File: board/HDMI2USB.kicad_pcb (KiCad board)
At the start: 10 copper layers, 337 parts, among them J1 USB_MICRO_B, P3 CONN_7X2, SW1 SW_PUSH, U1 MT41J128M16, U10 XC6SLX150T, U16 ΜA78L00, U17 FXO-HC536R, U18 FXO-HC536R, U19 FXO-HC536R, U20 KSZ9031RNX, U3 W25Q128FVEIG

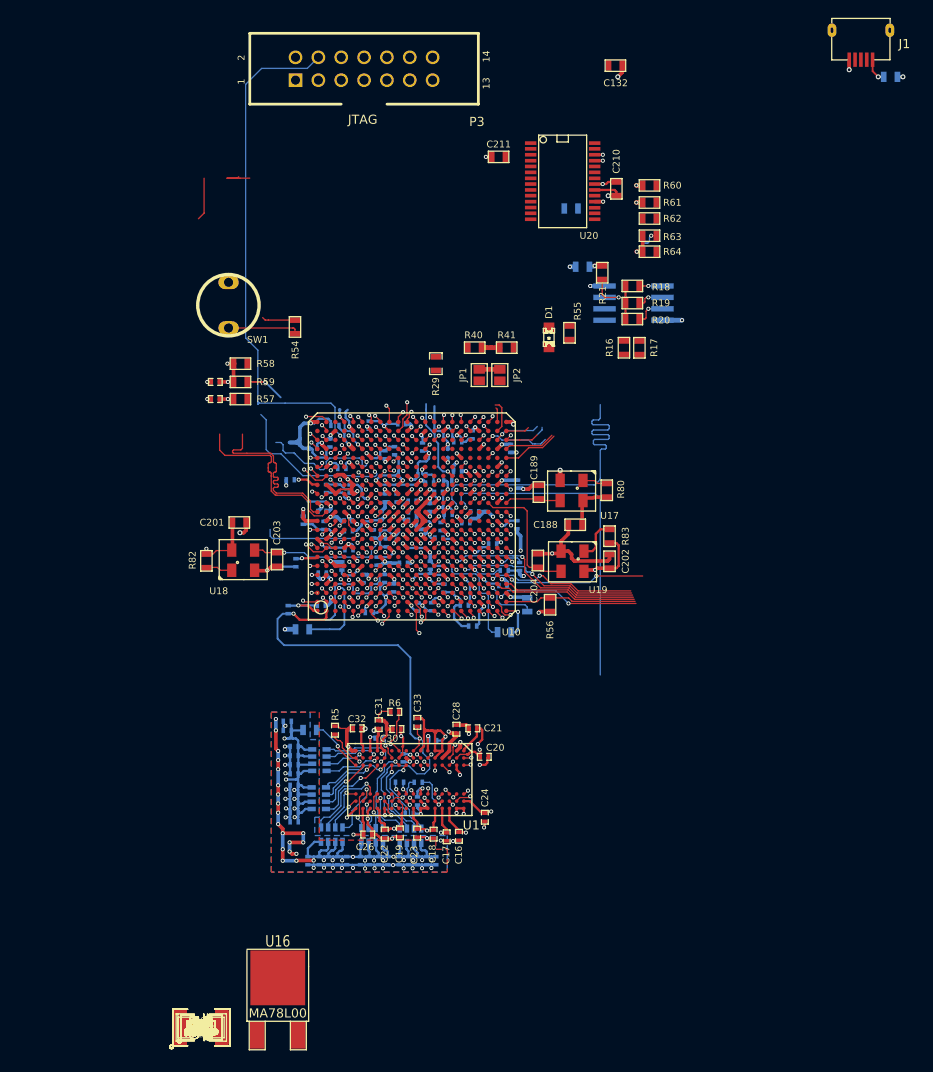
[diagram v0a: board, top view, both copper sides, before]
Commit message: Issue #1458 - HDMI RX TX pins added, Cypress added, DDR added
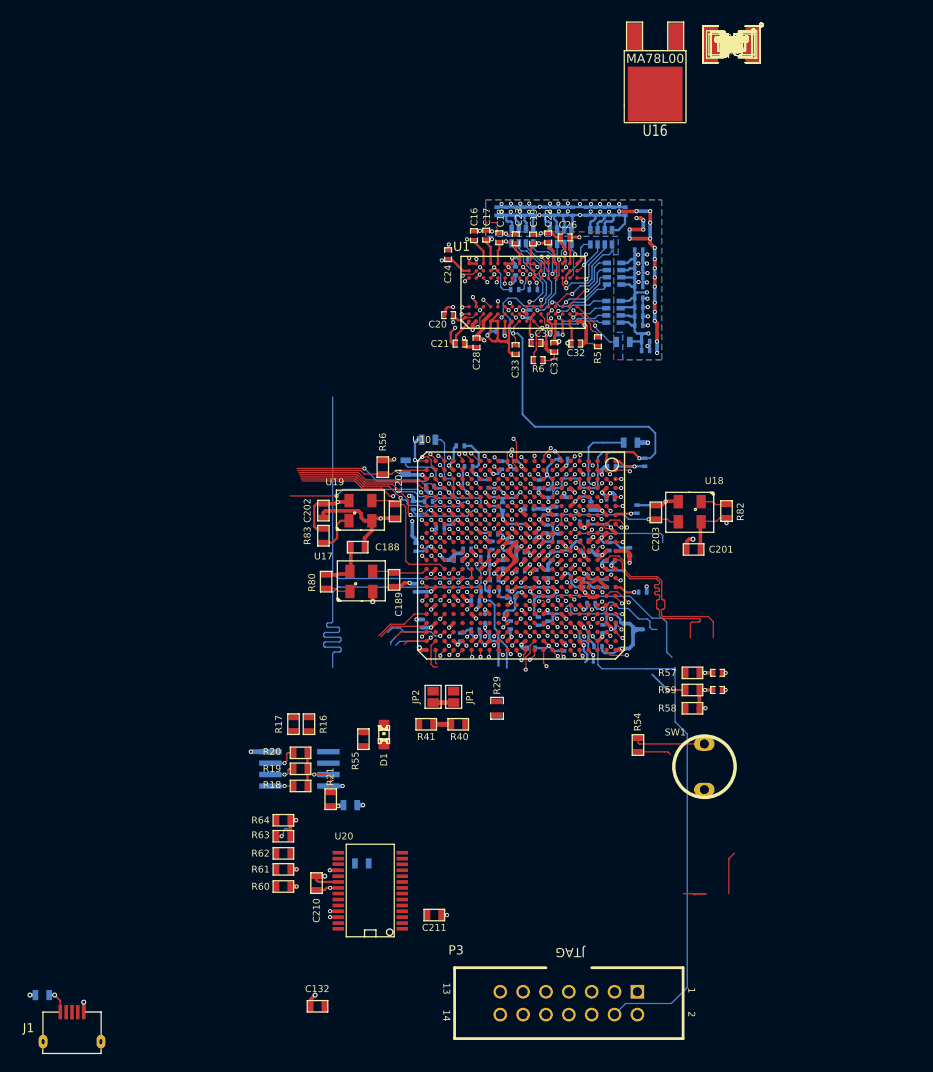
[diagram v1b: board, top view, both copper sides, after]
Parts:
- moved J1 142.6 mm to (162.8, 226.1), turned to 0 degrees
- moved R22 138.9 mm to (159.5, 220.9), turned to 0 degrees
- moved C133 124.2 mm to (236.1, 115.3), turned to 180 degrees
- moved C134 124.2 mm to (236.1, 115.3), turned to 180 degrees
- moved C135 124.2 mm to (236.1, 115.3), turned to 180 degrees
- moved C136 124.2 mm to (236.1, 115.3), turned to 180 degrees
- moved C137 124.2 mm to (236.1, 115.3), turned to 180 degrees
- moved C138 124.2 mm to (236.1, 115.3), turned to 180 degrees
- moved C139 124.2 mm to (236.1, 115.3), turned to 180 degrees
- moved C140 124.2 mm to (236.1, 115.3), turned to 180 degrees
- moved C141 124.2 mm to (236.1, 115.3), turned to 180 degrees
- moved C142 124.2 mm to (236.1, 115.3), turned to 180 degrees
- moved C143 124.2 mm to (236.1, 115.3), turned to 180 degrees
- moved C144 124.2 mm to (236.1, 115.3), turned to 180 degrees
- moved C145 124.2 mm to (236.1, 115.3), turned to 180 degrees
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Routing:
- net (no net): track 2011.9 -> 2009.5 mm

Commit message: Issue #1481 - DOC
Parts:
- removed R68: 100R, SM0402
- added D2: LED, DO214, F.Cu at (48.5, -14.2)
- added J2: HDMI, HDMI_TH, F.Cu at (195.6, 232.4)
- added J3: HDMI, HDMI_TH, F.Cu at (222.0, 232.4)
- added J4: HDMI, HDMI_TH, F.Cu at (139.4, 232.2)
- added J5: HDMI, HDMI_TH, F.Cu at (167.1, 232.4)
- added J6: RJ45(HFJ11-1GO1ERL), RJ45_10P-10C, F.Cu at (243.1, 82.3)
- added L1: INDUCTOR, SM0805, F.Cu at (212.1, 89.7)
- added L2: 7.2uH, IND202, F.Cu at (125.2, -24.1)
- added L4: 1.5UH, IND202, F.Cu at (60.2, -47.8)
- added L5: 1.5UH, IND202, F.Cu at (44.7, -26.2)
- added L6: INDUCTOR, SM0805, F.Cu at (212.1, 79.2)
- added L7: INDUCTOR, SM0805, F.Cu at (212.1, 84.3)
- added P1: CONN_2, pin_array_6x2_SMD, F.Cu at (40.8, -39.1)
- added P4: CONN_1, FX18_120, F.Cu at (37.7, -75.3)
- added P5: CONN_1, FX18_120, F.Cu at (37.2, -89.0)
- added P6: CONN_1, DIP-SMD_2X2, F.Cu at (108.0, -13.7)
- added R116: 10K, SM0603, F.Cu at (-24.9, 69.6)
- added R124: 50R, SM0603, F.Cu at (219.2, 205.2)
- added R125: 50R, SM0603, F.Cu at (217.2, 205.2)
- added R126: 100K, SM0603, F.Cu at (161.8, 208.8)
- added R127: 100K, SM0603, F.Cu at (191.8, 209.0)
- added R128: 50R, SM0603, F.Cu at (-4.83, 58.4)
- added R129: 47K, SM0603, F.Cu at (161.8, 206.5)
- added R130: 47K, SM0603, F.Cu at (189.7, 209.0)
- added R131: 50R, SM0603, F.Cu at (215.1, 205.2)
- added R132: 100K, SM0603, F.Cu at (213.4, 210.1)
- added R133: 47K, SM0603, F.Cu at (161.8, 204.5)
- added R134: 47K, SM0603, F.Cu at (187.7, 209.0)
- added R135: 47K, SM0603, F.Cu at (215.4, 210.1)
- added R136: 47K, SM0603, F.Cu at (217.4, 210.1)
- added R137: 1.5K, SM0603, F.Cu at (187.7, 205.2)
- added R138: 1.5K, SM0603, F.Cu at (158.5, 209.0)
- added R139: 1.5K, SM0603, F.Cu at (189.7, 205.2)
- added R140: 1.5K, SM0603, F.Cu at (158.5, 207.0)
- added R141: 1.5K, SM0603, F.Cu at (229.1, 208.5)
- added R142: 1.5K, SM0603, F.Cu at (227.1, 208.5)
- added R143: 27K, SM0603, F.Cu at (192.0, 205.2)
- added R144: 27K, SM0603, F.Cu at (158.5, 205.0)
- added R145: 50R, SM0603, F.Cu at (226.8, 205.2)
- added R146: 27K, SM0603, F.Cu at (231.1, 208.5)
- added R147: 50R, SM0603, F.Cu at (228.9, 205.2)
- added R148: 15K, SM0603, F.Cu at (194.1, 205.2)
- added R149: 15K, SM0603, F.Cu at (158.5, 202.9)
- added R150: 50R, SM0603, F.Cu at (230.9, 205.2)
- added R151: 15K, SM0603, F.Cu at (233.2, 208.5)
- added R152: 50R, SM0603, F.Cu at (232.9, 205.2)
- added R153: 1K, SM0603, F.Cu at (232.9, 229.9)
- added R188: 50R, SM0603, F.Cu at (129.8, 211.8)
- added R189: 50R, SM0603, F.Cu at (129.8, 209.8)
- added R190: 50R, SM0603, F.Cu at (129.8, 207.8)
- added R191: 50R, SM0603, F.Cu at (129.8, 205.7)
- added R192: 100K, SM0603, F.Cu at (125.2, 215.4)
- added R193: 47K, SM0603, F.Cu at (125.2, 217.4)
- added R194: 47K, SM0603, F.Cu at (125.2, 219.7)
- added R196: 1.5K, SM0603, F.Cu at (119.9, 223.5)
- added R197: 1.5K, SM0603, F.Cu at (119.6, 225.8)
- added R198: 50R, SM0603, F.Cu at (124.7, 223.8)
- added R199: 27K, SM0603, F.Cu at (119.6, 227.8)
- added R200: 50R, SM0603, F.Cu at (124.7, 225.8)
- added R201: 50R, SM0603, F.Cu at (124.7, 227.8)
- added R203: 50R, SM0603, F.Cu at (124.7, 230.1)
- added R204: 15K, SM0603, F.Cu at (119.6, 230.1)
- added R205: 1K, SM0603, F.Cu at (143.5, 225.8)
- added R66: 4.7K, SM0603, F.Cu at (235.7, 105.4)
- added R67: 4.7K, SM0603, F.Cu at (235.7, 109.2)
- added R72: 0R, SM0402, F.Cu at (35.3, -59.7)
- added R73: 390R, SM0603, F.Cu at (252.7, 113.3)
- added R74: 4.7K, SM0603, F.Cu at (252.7, 111.5)
- added R92: 330R, SM0603, F.Cu at (253.5, 78.2)
- added R93: 10K, SM0603, F.Cu at (-24.9, 63.0)
- added U11: MICRO_SD, MicroSD, F.Cu at (349.9, 32.3)
- added U12: TPS51200, BGA96-0.8, F.Cu at (28.0, -23.0)
- added U13: IP4776CZ38, SSOP38_N, F.Cu at (165.9, 217.9)
- added U14: IP4776CZ38, SSOP38_N, F.Cu at (194.1, 217.4)
- added U15: IP4776CZ38, SSOP38_N, F.Cu at (221.2, 217.7)
- added U2: CY7C68013A_100AC, PCI-EXPRESS, F.Cu at (-2.24, 75.7)
- added U21: IP4776CZ38, SSOP38_N, F.Cu at (138.4, 217.9)
- added U22: ΜA78L00, SSOP28, F.Cu at (-10.2, 46.0)
- added U4: GBU15005-G, PDSO_G14, F.Cu at (108.7, -40.6)
- added U5: 7805, PDSO_G14, F.Cu at (80.8, -43.9)
- added U6: TPS54560, SMAJACKRightAngled, F.Cu at (25.9, -41.7)
- added U7: TPS53319, DQP-22, F.Cu at (59.4, -28.2)
- added U8: TPS54625, PDSO_G14, F.Cu at (76.5, -25.9)
- added U9: TPS54625, SON_10, F.Cu at (59.7, -13.5)
- C201, C202, C53, C58: value 0.1UF -> 0.1MFD
- C203: value 15PF -> 4.7uF; footprint SM0603 -> SM0805
- C204: value 15PF -> 1uF; footprint SM0603 -> SM0805
- C210, C211: value 100nF -> 4.7uF; footprint SM0603 -> SM0805
- C212: value 100nF -> 4.7uF; footprint SM1210 -> SM0805
- C214, C217, C218, C219, C230: footprint SM1210 -> SM0805
- C216: value 100nF -> 27pF; footprint SM1210 -> SM0603
- C220: value 4.7uF -> 100nF; footprint SM1812 -> SM0805
- C222: value 100nF -> 0.1uF; footprint SM1812 -> SM0603
- C223: footprint SM0603 -> SM0805
- C225: value 100nF -> 4.7uF; footprint SM1812 -> SM0805
- C226, C229: footprint SM1210 -> SM0603; moved to B.Cu
- C227: footprint SM1812 -> SM0805
- C231: value 12pF -> 100nF; footprint SM1812 -> SM0805
- C232: value 12pF -> 100nF; footprint SM0805 -> SM0603; moved to B.Cu
- C233, C234: footprint SM0805 -> SM0603; moved to B.Cu
- C235: value 100nF -> 12pF; footprint SM0805 -> SM0603
- C238: value 100nF -> 12pF; footprint SM0402 -> SM0603
- C239: footprint SM0402 -> SM0603
- C39, C40, C41, C42: value 0.1MFD -> 0.1uFD
- C43, C44: value 12pF -> 0.1MFD
- C46, C49, C50: value 10UF -> 47uF
- C47: value 10UF -> 4.7uF
- C52: value 1UF -> 0.1MFD
- C54: value 8.2NF -> 0.1MFD
- C62: value 0.1UF -> 12pF
- C64: value 47UF -> 12pF
- C66: value 47UF -> 0.1MFD
- R13: value 10K -> 8.06K
- R14: value 10K -> 100R
- R15: value 10K -> 330R
- R16, R17: value R -> 50R
- R18, R19, R20, R21: value R -> 10K
- R22: value 4.7K -> 1K; moved to F.Cu
- R23, R24, R26: value 75R -> 100R
- R25: value 75R -> 100K
- R27, R28: value 75R -> 330R
- R30: value 75R -> 20K
- R31: value 75R -> 1.5K
- R32, R35, R36: value 75R -> 10K
- R33, R34: value 75R -> 2.2K
- R37, R49, R51: value 75R -> 4.7K
- R38: value 10K -> 39K
- R39: value 10K -> 27K
- R42, R43: value 1.5K -> 0R
- R44, R45: value 10K -> 0R
- R46: value 2.2K -> 0R
- R47: value 75R -> 0R
- R48: value 75R -> 4.7K; footprint SM0402 -> SM0603
- R50: value 2.2K -> 1.5K
- R65: value 100R -> 4.7K
- R69: value 100R -> 2.49K; footprint SM0402 -> SM0603
- R70: value 330R -> 390R; footprint SM0402 -> SM0603
- R71: value 330R -> 4.7K; footprint SM0402 -> SM0603
- R75: value 10K -> 4.7K; footprint SM0402 -> SM0603
- R76: value 100K -> 100R
- R81: value 21.5K -> 100R
- R82, R83: value 4K7 -> 100R
- R84: value 22.1K -> 100K; moved to B.Cu
- R88: value 0.03E -> 100K; moved to B.Cu
- R89: value 0.03E -> 330R
- U18: value FXO-HC536R -> USB3340
- U19: value FXO-HC536R -> MCP1825; footprint FXO-HC536R -> SOT223-5
- U20: value KSZ9031RNX -> RTL8211E-VB; footprint SSOP28 -> QFN48(RTL8211E)
- moved C40 187.1 mm to (75.2, 19.8)
- moved C42 180.8 mm to (82.5, 19.8)
- moved C41 177.0 mm to (82.5, 27.2)
- moved C44 172.5 mm to (92.5, 19.8)
- moved C63 168.9 mm to (91.9, 27.2)
- moved C37 166.7 mm to (99.8, 19.3)
- moved C65 162.7 mm to (99.8, 26.4)
- moved C38 161.5 mm to (106.4, 19.1)
- moved C179 156.3 mm to (121.7, 221.7)
- moved R88 150.7 mm to (143.5, 234.2)
- moved C76 149.6 mm to (121.9, 18.5)
- moved C185 145.5 mm to (143.5, 227.6)
- moved C133 142.8 mm to (121.4, 30.1)
- moved C134 142.8 mm to (121.4, 30.1)
- moved C135 142.8 mm to (121.4, 30.1)
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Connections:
- net /Cypress/D_N renamed /USB/USB_DM
- net /Cypress/D_P renamed /USB/USB_DP
- net N-00000500 renamed /USB/U1-SCL
- C136 pad 1: DDR1V8 -> VCC1V5
- C138 pad 2: DDR1V8 -> VCC1V5
- C154 pad 1: /Power/VCC3V3_RS+ -> VCC3V3
- C155 pad 2: /Power/DDR1V8_RS+ -> VCC1V5
- C156 pad 2: /Power/DDR0V9_RS+ -> VTTDDR0
- C157 pad 2: /Power/VCC3V3_RS+ -> VCC3V3
- C158 pad 1: /Power/VCC1V2_RS+ -> VCC1V2
- C159 pad 2: /Power/DDR0V9_RS+ -> VTTDDR0
- C160 pad 2: /Power/VCC3V3_RS+ -> VCC3V3
- C161 pad 2: /Power/DDR1V8_RS+ -> VCC1V5
- C162 pad 2: /Power/DDR0V9_RS+ -> VTTDDR0
- C163 pad 2: /Power/VCC3V3_RS+ -> VCC3V3
- C164 pad 2: /Power/VCC1V2_RS+ -> VCC1V2
- C165 pad 2: /Power/DDR1V8_RS+ -> VCC1V5
- C166 pad 2: /Power/DDR0V9_RS+ -> VTTDDR0
- C167 pad 2: /Power/VCC1V2_RS+ -> VCC1V2
- C168 pad 2: /Power/DDR0V9_RS+ -> VTTDDR0
- C189 pad 2: /SPI_Flash/USRCLK -> /FPGA_Bank_1_2/USRCLK
- C201 pad 1: GND -> VCC3V3
- C201 pad 2: VCC3V3 -> GND
- C202 pad 1: GND -> VCC3V3
- C202 pad 2: VCC3V3 -> GND
- C203 pad 1: GND -> /Ethernet/VCC3V3
- C203 pad 2: /SPI_Flash/CLK2 -> GND
- C204 pad 1: GND -> /Ethernet/VCC1V0
- C204 pad 2: /SPI_Flash/CLK1 -> GND
- C210 pad 1: /Ethernet/VCC1V2 -> /Ethernet/VCC3V3
- C211 pad 1: /Ethernet/VCC1V2 -> /Ethernet/VCC3V3
- C212 pad 1: /Ethernet/VCC1V2 -> /Ethernet/VCC1V0
- C214 pad 1: /Ethernet/VCC1V2 -> /Ethernet/ETH_VCC3V3
- C216 pad 1: /Ethernet/AVDDL -> GND
- C216 pad 2: GND -> /Ethernet/ETH_RXCLK
- C217 pad 1: /Ethernet/PLL1V2 -> /Ethernet/VCC3V3
- C218 pad 1: /Ethernet/VCC1V2 -> /Ethernet/VCC3V3
- C219 pad 1: /Ethernet/AVDDL -> /Ethernet/ETH_VCC3V3
- C220 pad 1: /Ethernet/PLL1V2 -> /Ethernet/ETH_VCC3V3
- C222 pad 1: /Ethernet/VCC1V2 -> /Ethernet/ETH_RESET_B
- C223 pad 1: /Ethernet/AVDDL -> /Ethernet/ETH_VCC1V0
- C224 pad 1: /Ethernet/AVDDH -> /Ethernet/AVDD3V3
- C225 pad 1: /Ethernet/DVDDH -> /Ethernet/ETH_VCC3V3
- C226 pad 1: /Ethernet/AVDDH -> /Ethernet/ETH_VCC1V0
- C227 pad 1: /Ethernet/DVDDH -> /Ethernet/AVDD3V3
- C228 pad 1: /Ethernet/AVDDH -> /Ethernet/ETH_VCC3V3
- C229 pad 1: /Ethernet/DVDDH -> /Ethernet/ETH_VCC1V0
- C230 pad 1: /Ethernet/AVDDH -> /Ethernet/AVDD3V3
- C231 pad 1: /Ethernet/XTAL2 -> /Ethernet/ETH_VCC3V3
- C232 pad 1: /Ethernet/XTAL1 -> /Ethernet/ETH_VCC1V0
- C233 pad 1: GND -> /Ethernet/ETH_VCC1V0
- C233 pad 2: N-00000461 -> GND
- C234 pad 1: GND -> /Ethernet/ETH_VCC1V0
- C234 pad 2: N-00000460 -> GND
- C235 pad 1: GND -> /Ethernet/XTAL2_50MHZ
- C235 pad 2: N-00000459 -> GND
- C238 pad 1: GND -> /Ethernet/XTAL1_50MHZ
- C238 pad 2: N-00000458 -> GND
- C239 pad 1: /Ethernet/C_GND -> /Ethernet/VCC3V3
- C34 pad 1: VCC3V3 -> N-00000381
- C35 pad 1: VCC3V3 -> N-00000381
- C37 pad 1: VCC3V3 -> GND
- C37 pad 2: GND -> N-00000375
- C38 pad 1: VCC3V3 -> N-00000364
- C43 pad 1: GND -> VCC3V3
- C43 pad 2: N-00000503 -> GND
- C44 pad 1: N-00000502 -> VCC3V3
- C46 pad 1: VCC12V0 -> GND
- C46 pad 2: GND -> N-00000399
- C47 pad 2: VCC12V0 -> N-00000399
- C49 pad 2: VCC12V0 -> VCC5V0
- C50 pad 1: VCC12V0 -> GND
- C50 pad 2: GND -> VCC5V0
- C52 pad 1: GND -> VCC3V3
- C52 pad 2: N-00000539 -> GND
- C53 pad 1: VCC12V0 -> VCC3V3
- C54 pad 1: GND -> VCC3V3
- C54 pad 2: N-00000531 -> GND
- C58 pad 1: N-00000511 -> VCC3V3
- C58 pad 2: N-00000510 -> GND
- C62 pad 1: N-00000527 -> GND
- C62 pad 2: /Power/VCC5V0_RS+ -> /USB/XTALIN
- C64 pad 1: GND -> /USB/XTALIOUT
- C64 pad 2: /Power/VCC5V0_RS+ -> GND
- C66 pad 1: GND -> VCC3V3
- C66 pad 2: /Power/VCC5V0_RS+ -> GND
- C76 pad 2: DDR1V8 -> VCC1V5
- J1 pad 4: (no net) -> /USB/ID
- P3 pad 10: (no net) -> N-00000159
- P3 pad 4: (no net) -> N-00000152
- P3 pad 6: (no net) -> N-00000155
- P3 pad 8: (no net) -> N-00000157
- R13 pad 1: VCC3V3 -> GND
- R13 pad 2: N-00000492 -> N-00000365
- R14 pad 1: VCC3V3 -> N-00000374
- R14 pad 2: N-00000507 -> /FPGA_Power/TDO_FPGA/TDO-JTAG
- R15 pad 1: VCC3V3 -> N-00000369
- R15 pad 2: N-00000491 -> /FPGA_Power/PROG_B
- R16 pad 2: (no net) -> /FPGA_Bank_1_2/SPI_DO_DIN_MISO1
- R17 pad 2: (no net) -> /FPGA_Bank_1_2/SPI_D1_MISO2
- R18 pad 2: /SPI_Flash/SPI_CS_N -> /FPGA_Bank_1_2/SPI_CS_N
- R21 pad 1: /SPI_Flash/SPI_D2_MISO3 -> /FPGA_Bank_1_2/SPI_D2_MISO3
- R22 pad 1: GND -> N-00000337
- R22 pad 2: N-00000442 -> /Ethernet/VCC3V3
- R23 pad 2: (no net) -> /USB/TDO-USB/TDI-FPGA
- R24 pad 2: (no net) -> /FPGA_Power/TMS
- R25 pad 2: (no net) -> GND
- R26 pad 2: (no net) -> /FPGA_Power/TCK
- R27 pad 2: (no net) -> /FPGA_Power/INIT_B
- R28 pad 2: (no net) -> /FPGA_Power/DONE
- R30 pad 2: (no net) -> N-00000364
- R31 pad 2: (no net) -> N-00000373
- R32 pad 1: N-00000492 -> N-00000362
- R32 pad 2: (no net) -> GND
- R33 pad 1: N-00000491 -> /USB/U1-SDA
- R33 pad 2: (no net) -> VCC3V3
- R34 pad 2: (no net) -> VCC3V3
- R35 pad 1: N-00000498 -> N-00000343
- R35 pad 2: (no net) -> VCC3V3
- R36 pad 1: N-00000499 -> GND
- R36 pad 2: (no net) -> N-00000344
- R37 pad 1: N-00000490 -> N-00000363
- R37 pad 2: (no net) -> GND
- R38 pad 1: GND -> N-00000336
- R38 pad 2: N-00000490 -> /Ethernet/VCC1V0
- R39 pad 2: N-00000501 -> N-00000336
- R42 pad 1: N-00000505 -> /Ethernet/ETH_RXD0
- R42 pad 2: N-00000507 -> N-00000343
- R43 pad 1: N-00000506 -> /Ethernet/ETH_RXD1
- R43 pad 2: N-00000501 -> N-00000329
- R44 pad 1: VCC3V3 -> /Ethernet/ETH_RXD2
- R44 pad 2: /Cypress/U1-SLWR -> N-00000328
- R45 pad 1: VCC3V3 -> /Ethernet/ETH_RXD3
- R45 pad 2: /Cypress/U1-SLRD -> N-00000318
- R46 pad 1: /Cypress/U1-SCL -> /Ethernet/ETH_RXCTL
- R46 pad 2: VCC3V3 -> N-00000311
- R47 pad 1: N-00000480 -> (no net)
- R47 pad 2: (no net) -> N-00000317
- R48 pad 1: N-00000479 -> GND
- R48 pad 2: (no net) -> /Ethernet/ETH_RXCTL
- R49 pad 1: N-00000485 -> /Ethernet/ETH_VCC3V3
- R49 pad 2: (no net) -> /Ethernet/ETH_RXD0
- R50 pad 1: /Cypress/U1-SDA -> /Ethernet/ETH_VCC3V3
- R50 pad 2: VCC3V3 -> /Ethernet/ETH_MDIO
- R51 pad 1: (no net) -> /Ethernet/ETH_RESET_B
- R51 pad 2: N-00000496 -> /Ethernet/VCC3V3
- R52 pad 2: (no net) -> /FPGA_Power/INIT_B
- R56 pad 1: /FPGA_Power/FPGA_PROG_B -> /FPGA_Power/PROG_B
- R60 pad 1: /SPI_Flash/SD_DAT2 -> /FPGA_Bank_1_2/SD_DAT2
- R61 pad 1: /SPI_Flash/SD_DAT3 -> /FPGA_Bank_1_2/SD_DAT3
- R62 pad 1: /SPI_Flash/SD_CMD -> /FPGA_Bank_1_2/SD_CMD
- R63 pad 1: /SPI_Flash/SD_DAT0 -> /FPGA_Bank_1_2/SD_DAT0
- R64 pad 1: /SPI_Flash/SD_DAT1 -> /FPGA_Bank_1_2/SD_DAT1
- R65 pad 1: N-00000477 -> /Ethernet/ETH_VCC3V3
- R65 pad 2: (no net) -> /Ethernet/ETH_RXD1
- R69 pad 1: N-00000471 -> N-00000311
- R69 pad 2: (no net) -> GND
- R70 pad 1: N-00000473 -> N-00000321
- R70 pad 2: (no net) -> /Ethernet/LED0
- R71 pad 1: N-00000469 -> N-00000321
- R71 pad 2: (no net) -> /Ethernet/VCC3V3
- R75 pad 1: VCC12V0 -> N-00000331
- R75 pad 2: N-00000530 -> /Ethernet/VCC3V3
- R76 pad 1: N-00000539 -> N-00000152
- R76 pad 2: N-00000529 -> (no net)
- R81 pad 1: /Power/VCC5V0_RS+ -> N-00000155
- R81 pad 2: N-00000527 -> (no net)
- R82 pad 1: VCC3V3 -> N-00000157
- R82 pad 2: N-00000158 -> (no net)
- R83 pad 1: VCC3V3 -> N-00000159
- R83 pad 2: N-00000156 -> (no net)
- R84 pad 1: N-00000527 -> GND
- R84 pad 2: GND -> N-00000433
- R86 pad 2: N-00000442 -> /Ethernet/XTAL1_50MHZ
- R88 pad 1: VCC5V0 -> GND
- R88 pad 2: /Power/VCC5V0_RS+ -> N-00000432
- R89 pad 1: VCC5V0 -> N-00000325
- R89 pad 2: /Power/VCC5V0_RS+ -> GND
- U10 pad A14: (no net) -> /DisplayPort/TX_LANEN2
- U10 pad A16: (no net) -> /DisplayPort/TX_LANEN3
- U10 pad A18: (no net) -> /DisplayPort/RXCONFIG1
- U10 pad A19: (no net) -> /FPGA_Bank_0_3/TXHPD
- U10 pad A2: (no net) -> /FPGA_Bank_0_3/USB_D3
- U10 pad A20: (no net) -> /DisplayPort/TXAUXCH_N
- U10 pad A21: (no net) -> /FPGA_Power/TCK
- U10 pad A3: (no net) -> /FPGA_Bank_0_3/USB_RESETB
- U10 pad A4: (no net) -> /FPGA_Bank_0_3/USB_DIR
- U10 pad A6: (no net) -> /DisplayPort/TX_LANEN0
- U10 pad A8: (no net) -> /DisplayPort/TX_LANEN1
- U10 pad AA10: (no net) -> /HDMI/TMDS-TX1-1_P
- U10 pad AA16: (no net) -> /HDMI/TMDS-TX2-1_P
- U10 pad AA18: (no net) -> /HDMI/TMDS-TX2-HOT
- U10 pad AA20: (no net) -> /FPGA_Bank_1_2/SPI_DO_DIN_MISO1
- U10 pad AA3: (no net) -> /FPGA_Bank_1_2/SPI_CS_N
- U10 pad AA4: (no net) -> /FPGA_Bank_1_2/SD_DAT2
- U10 pad AA6: (no net) -> /Ethernet/ETH_TXD2
- U10 pad AA8: (no net) -> /HDMI/TMDS-TX1-SCL
- U10 pad AB10: (no net) -> /HDMI/TMDS-TX1-1_N
- U10 pad AB11: (no net) -> /HDMI/TMDS-TX1-CLK_N
- U10 pad AB13: (no net) -> /FPGA_Bank_1_2/USRCLK
- U10 pad AB15: (no net) -> /HDMI/TMDS-TX2-0_N
- U10 pad AB16: (no net) -> /HDMI/TMDS-TX2-1_N
- U10 pad AB17: (no net) -> /HDMI/TMDS-TX2-SDA
- U10 pad AB18: (no net) -> /HDMI/TMDS-TX2-CEC
- U10 pad AB2: /FPGA_Power/FPGA_PROG_B -> /FPGA_Power/PROG_B
- U10 pad AB20: (no net) -> /FPGA_Bank_1_2/SPI_MOSI_CSI_N_MISO0
- U10 pad AB4: (no net) -> /FPGA_Bank_1_2/SD_DAT3
- U10 pad AB5: (no net) -> /FPGA_Bank_1_2/SD_DAT1
- U10 pad AB6: (no net) -> /Ethernet/ETH_TXD3
- U10 pad AB7: (no net) -> /HDMI/TMDS-TX1-HOT
- U10 pad AB8: (no net) -> /HDMI/TMDS-TX1-SDA
- U10 pad AB9: (no net) -> /HDMI/TMDS-TX1-2_N
- U10 pad B14: (no net) -> /DisplayPort/TX_LANEP2
- U10 pad B16: (no net) -> /DisplayPort/TX_LANEP3
- U10 pad B18: (no net) -> /DisplayPort/RXCONFIG2
- U10 pad B2: (no net) -> /FPGA_Bank_0_3/USB_D4
- U10 pad B20: (no net) -> /DisplayPort/TXAUXCH_P
- U10 pad B3: (no net) -> /FPGA_Bank_0_3/USB_D0
- U10 pad B6: (no net) -> /DisplayPort/TX_LANEP0
- U10 pad B8: (no net) -> /DisplayPort/TX_LANEP1
- U10 pad C13: (no net) -> /DisplayPort/RX_LANEN2
- U10 pad C15: (no net) -> /DisplayPort/RX_LANEN3
- U10 pad C18: (no net) -> /DisplayPort/TXCONFIG1
- U10 pad C19: (no net) -> /FPGA_Bank_0_3/RXHPD
- U10 pad C4: (no net) -> /FPGA_Bank_0_3/USB_STP
- U10 pad C7: (no net) -> /DisplayPort/RX_LANEN0
- U10 pad C9: (no net) -> /DisplayPort/RX_LANEN1
- U10 pad D13: (no net) -> /DisplayPort/RX_LANEP2
- U10 pad D15: (no net) -> /DisplayPort/RX_LANEP3
- U10 pad D17: (no net) -> /DisplayPort/TXCONFIG2
- U10 pad D18: (no net) -> /DisplayPort/RXAUXCH_P
- U10 pad D20: (no net) -> /FPGA_Power/TMS
- U10 pad D3: (no net) -> /FPGA_Bank_0_3/USB_D7
- U10 pad D4: (no net) -> /FPGA_Bank_0_3/USB_D6
- U10 pad D5: (no net) -> /FPGA_Bank_0_3/USB_D5
- U10 pad D7: (no net) -> /DisplayPort/RX_LANEP0
- U10 pad D9: (no net) -> /DisplayPort/RX_LANEP1
- U10 pad E18: (no net) -> /USB/TDO-USB/TDI-FPGA
- U10 pad E5: (no net) -> /FPGA_Bank_0_3/USB_D2
- U10 pad E6: (no net) -> /FPGA_Bank_0_3/USB_D1
- U10 pad E9: (no net) -> GTP1V2
- U10 pad F7: (no net) -> /FPGA_Bank_0_3/USB_NXT
- U10 pad G17: (no net) -> /FPGA_Power/TDO_FPGA/TDO-JTAG
- U10 pad G9: (no net) -> /FPGA_Bank_0_3/USB_REFCLK
- U10 pad H21: (no net) -> /HDMI/TMDS-RX1-SCL
- U10 pad H22: (no net) -> /HDMI/TMDS-RX1-SDA
- U10 pad J20: (no net) -> /HDMI/TMDS-RX1-1_P
- U10 pad J22: (no net) -> /HDMI/TMDS-RX1-1_N
- U10 pad K17: (no net) -> /HDMI/TMDS-RX2-HOT
- U10 pad K20: (no net) -> /HDMI/TMDS-RX1-2_P
- U10 pad K21: (no net) -> /HDMI/TMDS-RX1-CLK_P
- U10 pad K22: (no net) -> /HDMI/TMDS-RX1-CLK_N
- U10 pad L17: (no net) -> /HDMI/TMDS-RX1-CEC
- U10 pad L19: (no net) -> /HDMI/TMDS-RX1-2_N
- U10 pad L20: (no net) -> /HDMI/TMDS-RX2-CLK_P
- U10 pad L22: (no net) -> /HDMI/TMDS-RX2-CLK_N
- U10 pad M19: (no net) -> /HDMI/TMDS-RX1-0_N
- U10 pad M20: (no net) -> /HDMI/TMDS-RX1-0_P
- U10 pad M21: (no net) -> /HDMI/TMDS-RX2-0_P
- U10 pad M22: (no net) -> /HDMI/TMDS-RX2-0_N
- U10 pad N20: (no net) -> /HDMI/TMDS-RX2-1_P
- U10 pad N22: (no net) -> /HDMI/TMDS-RX2-1_N
- U10 pad P21: (no net) -> /HDMI/TMDS-RX2-2_P
- U10 pad P22: (no net) -> /HDMI/TMDS-RX2-2_N
- U10 pad R13: (no net) -> /FPGA_Bank_1_2/SPI_D1_MISO2
- U10 pad R20: (no net) -> /HDMI/TMDS-RX2-SCL
- U10 pad R22: (no net) -> /HDMI/TMDS-RX2-SDA
- U10 pad R8: (no net) -> /Ethernet/ETH_RXD1
- U10 pad R9: (no net) -> /Ethernet/ETH_RXD0
- U10 pad T10: (no net) -> /Ethernet/MAC_SDA
- U10 pad T12: (no net) -> /HDMI/TMDS-TX2-CLK_P
- U10 pad T14: (no net) -> /FPGA_Bank_1_2/SPI_D2_MISO3
- U10 pad T21: (no net) -> /HDMI/TMDS-RX2-CEC
- U10 pad T22: (no net) -> /HDMI/TMDS-RX1-HOT
- U10 pad T7: (no net) -> /FPGA_Bank_1_2/SD_CMD
- U10 pad T8: (no net) -> /Ethernet/ETH_RESET_B
- U10 pad U12: (no net) -> /HDMI/TMDS-TX2-CLK_N
- U10 pad U13: (no net) -> /HDMI/TMDS-TX2-2_N
- U10 pad U14: (no net) -> /HDMI/TMDS-TX2-2_P
- U10 pad U6: (no net) -> /FPGA_Bank_1_2/SD_CLK
- U10 pad U8: (no net) -> /Ethernet/ETH_MDIO
- U10 pad U9: (no net) -> /Ethernet/ETH_RXCTL
- U10 pad V7: (no net) -> /Ethernet/ETH_MDC
- U10 pad V9: (no net) -> /Ethernet/ETH_INT_B
- U10 pad W12: (no net) -> /HDMI/TMDS-TX1-0_P
- U10 pad W6: (no net) -> /Ethernet/ETH_RXD2
- U10 pad W8: (no net) -> /Ethernet/ETH_TXCTL
- U10 pad W9: (no net) -> /Ethernet/ETH_TXD0
- U10 pad Y11: (no net) -> /HDMI/TMDS-TX1-CLK_P
- U10 pad Y12: (no net) -> /HDMI/TMDS-TX1-0_N
- U10 pad Y15: (no net) -> /HDMI/TMDS-TX2-0_P
- U10 pad Y17: (no net) -> /HDMI/TMDS-TX2-SCL
- U10 pad Y20: (no net) -> /FPGA_Bank_1_2/SPI_CLK
- U10 pad Y5: (no net) -> /FPGA_Bank_1_2/SD_DAT0
- U10 pad Y6: (no net) -> /Ethernet/ETH_RXD3
- U10 pad Y7: (no net) -> /HDMI/TMDS-TX1-CEC
- U10 pad Y8: (no net) -> /Ethernet/ETH_TXD1
- U10 pad Y9: (no net) -> /HDMI/TMDS-TX1-2_P
- U17 pad 3: /SPI_Flash/USRCLK -> /FPGA_Bank_1_2/USRCLK
- U18 pad 1: N-00000158 -> VCC3V3
- U18 pad 2: GND -> /FPGA_Bank_0_3/USB_NXT
- U18 pad 3: /SPI_Flash/CLK2 -> /FPGA_Bank_0_3/USB_D0
- U18 pad 4: VCC3V3 -> /FPGA_Bank_0_3/USB_D1
- U19 pad 1: N-00000156 -> N-00000337
- U19 pad 2: GND -> /Ethernet/VCC3V3
- U19 pad 3: /SPI_Flash/CLK1 -> GND
- U19 pad 4: VCC3V3 -> /Ethernet/VCC1V0
- U20 pad 1: /Ethernet/AVDDH -> N-00000332
- U20 pad 10: N-00000457 -> N-00000328
- U20 pad 12: /Ethernet/AVDDH -> (no net)
- U20 pad 13: N-00000455 -> /Ethernet/ETH_RXCTL
- U20 pad 14: /Ethernet/VCC1V2 -> /Ethernet/ETH_RXD0
- U20 pad 15: /Ethernet/LED2 -> /Ethernet/ETH_VCC3V3
- U20 pad 16: /Ethernet/DVDDH -> /Ethernet/ETH_RXD1
- U20 pad 17: /Ethernet/LED1 -> /Ethernet/ETH_RXD2
- U20 pad 18: /Ethernet/VCC1V2 -> /Ethernet/ETH_RXD3
- U20 pad 19: (no net) -> /Ethernet/ETH_RXCLK
- U20 pad 20: (no net) -> /Ethernet/ETH_INT_B
- U20 pad 21: (no net) -> /Ethernet/ETH_VCC3V3
- U20 pad 23: /Ethernet/VCC1V2 -> /Ethernet/ETH_TXD0
- U20 pad 24: (no net) -> /Ethernet/ETH_TXD1
- U20 pad 25: (no net) -> /Ethernet/ETH_TXD2
- U20 pad 26: /Ethernet/VCC1V2 -> /Ethernet/ETH_TXD3
- U20 pad 27: (no net) -> /Ethernet/ETH_TXCTL
- U20 pad 28: (no net) -> /Ethernet/ETH_VCC1V0
- U20 pad 3: N-00000466 -> /Ethernet/ETH_VCC1V0
- U20 pad 4: /Ethernet/AVDDL -> N-00000312
- U20 pad 6: N-00000465 -> /Ethernet/AVDD3V3
- U20 pad 9: /Ethernet/AVDDL -> /Ethernet/ETH_VCC1V0
- U3 pad 1: /SPI_Flash/SPI_CS_N -> /FPGA_Bank_1_2/SPI_CS_N
- U3 pad 5: (no net) -> /FPGA_Bank_1_2/SPI_MOSI_CSI_N_MISO0
- U3 pad 6: (no net) -> /FPGA_Bank_1_2/SPI_CLK
- U3 pad 7: /SPI_Flash/SPI_D2_MISO3 -> /FPGA_Bank_1_2/SPI_D2_MISO3
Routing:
- net (no net): track 2009.5 -> 1103.0 mm, vias 217 -> 118
- net /FPGA_Power/TMS: track 0.00 -> 49.2 mm, vias 0 -> 1
- net /HDMI/TMDS-TX2-CLK_N: track 0.00 -> 37.7 mm, vias 0 -> 1
- net /HDMI/TMDS-TX2-CLK_P: track 0.00 -> 37.7 mm, vias 0 -> 1
- net /FPGA_Bank_0_3/USB_D1: track 0.00 -> 25.5 mm, vias 0 -> 1
- net /FPGA_Bank_1_2/SD_CMD: track 0.00 -> 23.1 mm, vias 0 -> 2
- net /Ethernet/ETH_RXD1: track 0.00 -> 22.9 mm, vias 0 -> 1
- net /Ethernet/ETH_RXD0: track 0.00 -> 22.2 mm, vias 0 -> 1
- net /FPGA_Bank_1_2/SD_CLK: track 0.00 -> 20.7 mm, vias 0 -> 2
- net /FPGA_Bank_0_3/USB_D7: track 0.00 -> 20.0 mm, vias 0 -> 1
- net /FPGA_Bank_0_3/USB_D2: track 0.00 -> 20.0 mm, vias 0 -> 1
- net /FPGA_Bank_0_3/USB_NXT: track 0.00 -> 19.8 mm, vias 0 -> 2
- net /DisplayPort/TX_LANEN1: track 0.00 -> 19.2 mm, vias 0 -> 1
- net /FPGA_Bank_0_3/USB_D5: track 0.00 -> 19.2 mm, vias 0 -> 1
- net /DisplayPort/TX_LANEP1: track 0.00 -> 19.2 mm, vias 0 -> 1
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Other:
- board outline added: 191.8 x 91.4 mm

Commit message: Issue #1481 - GPIO sheet
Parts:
- removed C240: 100nF, SM0201_r
- removed R42, R43, R44, R45, R47: 0R, SM0603
- removed R46: 0R, SM0402
- added R100, R103, R111: 10K, SM0603, F.Cu at (282.8, 179.3)
- added R101, R105: 10K, SM0402, F.Cu at (282.8, 179.3)
- added R102, R104, R106, R107, R108, R109: 100K, SM0603, F.Cu at (282.8, 179.3)
- added R110: 46.4K, SM0603, F.Cu at (282.8, 179.3)
- added R112: 21.5K, SM0603, F.Cu at (282.8, 179.3)
- added R113, R115: 22.1K, SM0603, F.Cu at (282.8, 179.3)
- added R114: 12.7K, SM0603, F.Cu at (282.8, 179.3)
- added R95: 200K, SM0603, F.Cu at (282.8, 179.3)
- added R96: 86.6K, SM0603, F.Cu at (282.8, 179.3)
- added R97: 1K, SM0603, F.Cu at (282.8, 179.3)
- added R98: 205K, SM0603, F.Cu at (282.8, 179.3)
- added R99: ?, SM0603, F.Cu at (282.8, 179.3)
- added X2: 50MHz, HC-49V, F.Cu at (119.9, 123.2)
- C148, C149: footprint SM0402 -> SM0603
- C151, C154: footprint SM0402 -> SM0805
- C157, C160, C163: footprint SM0402 -> SM1210
- C222, C235, C238, R70, R73: moved to B.Cu
- C72, C73, C74: footprint SM0805 -> SM1210
- C75: footprint SM1812 -> SM1210
- C77: footprint SM1812 -> SM0603
- J1: footprint MICRO_USB_B -> MICRO_USB_B_N
- U12: footprint BGA96-0.8 -> SON_10(tps51200)
- U16: footprint DPAK2 -> μA78L00
- U18: footprint FXO-HC536R -> QFN-32(USB3340)
- U2: footprint PCI-EXPRESS -> TQFP-100_(CY7C68013A-100AXC)
- U22: footprint SSOP28 -> μA78L00
- U5: footprint PDSO_G14 -> DPAK2
- U7: footprint DQP-22 -> DQP-22(tps53319)
- U8: footprint PDSO_G14 -> PDSO_G14(tps54625)
- U9: footprint SON_10 -> PDSO_G14(tps54625)
- moved L2 320.4 mm to (277.9, 257.5)
- moved U12 280.2 mm to (302.0, 35.8)
- moved U2 270.1 mm to (263.2, 125.5), turned to 90 degrees
- moved U7 267.8 mm to (319.3, 36.6)
- moved U9 255.3 mm to (310.4, 35.1)
- moved C60 250.9 mm to (262.5, 251.8)
- moved U8 248.3 mm to (319.3, 25.9)
- moved R72 194.6 mm to (119.2, 115.9)
- moved U18 167.1 mm to (319.3, 48.5)
- moved C203 138.5 mm to (52.7, 105.6)
- moved C204 138.5 mm to (55.2, 105.6)
- moved C210 138.5 mm to (68.7, 96.2)
- moved C211 138.5 mm to (68.7, 101.2)
- moved C212 138.5 mm to (71.2, 106.6)
- moved C217 138.5 mm to (71.2, 96.2)
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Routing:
- net GND: track 318.1 -> 341.1 mm, vias 118 -> 152
- net N-00000333: track 0.00 -> 17.9 mm
- net N-00000323: track 0.00 -> 17.9 mm
- net N-00000314: track 0.00 -> 17.9 mm, vias 0 -> 1
- net N-00000332: track 0.00 -> 17.9 mm
- net N-00000328: track 0.00 -> 17.9 mm
- net N-00000312: track 0.00 -> 17.8 mm, vias 0 -> 1
- net N-00000313: track 0.00 -> 17.8 mm
- net N-00000327: track 0.00 -> 17.8 mm
- net /HDMI/P1-CEC: track 0.00 -> 17.2 mm
- net /HDMI/P1-SDA: track 0.00 -> 15.7 mm
- net /HDMI/P1-HOT: track 0.00 -> 15.3 mm
- net /HDMI/P1-SCL: track 0.00 -> 15.2 mm
- net /FPGA_Bank_0_3/USB_D0: track 19.1 -> 4.49 mm, vias 2 -> 1
- net /HDMI/TMDS-RX1-CLK_P: track 4.17 -> 18.8 mm
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
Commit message: Issue #1481 - Placement
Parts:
- added C79: 10UF, SM1210, B.Cu at (277.1, 195.8)
- added C81: 10UF, SM0805, F.Cu at (264.9, 224.5)
- added D5: DIODE, B560C-SMC, F.Cu at (266.2, 118.9)
- added L3: 2.2UH, IND202, F.Cu at (262.4, 180.1)
- added P10, P11, P12, P13, P2, P7, P8, P9: CONN_1, 1pin, F.Cu at (388.3, 56.5)
- added R90: 143K, SM0603_Resistor, F.Cu at (251.2, 125.7)
- added R91: 10.2K, SM0603_Resistor, F.Cu at (251.2, 122.2)
- C133, C140: footprint SM0402 -> SM1206
- C134, C135, C69: footprint SM0402 -> SM1210; moved to B.Cu
- C136, C143, C144, C159, C166: footprint SM0402 -> SM0805; moved to B.Cu
- C137, C141: footprint SM0402 -> SM0603; moved to B.Cu
- C138, C147, C150, C152, C153, C156, C162: footprint SM0402 -> SM0805
- C139, C145: footprint SM0402 -> SM1210
- C142, C155, C158: footprint SM0402 -> SM0603
- C149, C160, C168, C201, C39, C43, C54, C66, C74, C75, R102, R104, R107, R95, R96, R97, R98, R99: moved to B.Cu
- C161, C164, C165: footprint SM0402 -> SM1812
- C167: footprint SM0805 -> SM1812
- C34, C35: footprint SM0201_r -> SM0603
- C37: footprint SM1210 -> SM0603
- C40, C41, C42, C44: footprint SM1210 -> SM0603; moved to B.Cu
- C45, C51, C56: footprint SM0603 -> SM1210; moved to B.Cu
- C48, C55: footprint SM0603 -> SM1210
- C52, C53: footprint SM0805 -> SM0603; moved to B.Cu
- C57: footprint SM1812 -> SM1210
- C58: footprint SM1812 -> SM0603; moved to B.Cu
- C60: footprint SM0805 -> SM0603_Capa
- C63: footprint SM1210 -> SM0603_Capa
- C65: footprint SM1206 -> SM0603_Capa
- C67, C68, C70, C78: footprint SM0805 -> SM1210
- C71: footprint SM0805 -> SM1210; moved to B.Cu
- C80: footprint SM0805 -> SM0603
- J1: footprint MICRO_USB_B_N -> USB_A
- L2: footprint IND202 -> Power_Inductor
- P4, P5: footprint FX18_120 -> 1pin
- P6: footprint DIP-SMD_2X2 -> 1pin
- R77, R78: footprint SM0402 -> SM0603_Capa
- R79: footprint SM0603 -> SM0603_Capa
- U4: footprint PDSO_G14 -> GBJ15005
- U6: footprint SMAJACKRightAngled -> TPS54560
- moved P4 372.1 mm to (382.9, 63.7)
- moved P5 372.1 mm to (382.4, 49.9)
- moved P1 349.4 mm to (364.2, 93.2)
- moved D2 337.9 mm to (365.8, 102.1)
- moved R116 327.8 mm to (337.8, 96.8)
- moved R128 327.8 mm to (349.8, 91.9)
- moved R93 327.8 mm to (337.8, 90.2)
- moved U22 327.8 mm to (343.2, 94.0)
- moved L5 315.9 mm to (261.9, 203.2), turned to 180 degrees
- moved U4 303.9 mm to (384.6, 86.9)
- moved U5 303.9 mm to (356.6, 83.6)
- moved L4 285.1 mm to (265.2, 150.4), turned to 180 degrees
- moved U6 280.9 mm to (256.5, 118.6), turned to 180 degrees
- moved P6 274.9 mm to (374.1, 54.9)
- moved C76 248.2 mm to (260.4, 224.5), turned to 90 degrees
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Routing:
- net (no net): track 1106.5 -> 1089.6 mm, vias 120 -> 112
- net GND: track 341.1 -> 338.1 mm, vias 152 -> 151
- net VCC3V3: track 105.0 -> 103.3 mm, vias 38 -> 37
- net /USB/USB_DP: track 1.28 -> 0.00 mm
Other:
- board size 191.8 x 91.4 mm -> 170 x 170 mm

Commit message: Issue #1481 - Placement
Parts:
- added CON1: BARREL_JACK, BARREL_JACK, F.Cu at (269.2, 67.8)
- added CON2: BARREL_JACK, BARREL_JACK, F.Cu at (242.1, 67.6)
- added F1: FUSE, SM2512, F.Cu at (318.5, 237.5)
- added F2: FUSE, SM2512, F.Cu at (333.8, 237.5)
- added F3: FUSE, SM2512, F.Cu at (318.3, 248.7)
- added J7: USB_MICRO_B, MICRO_USB_B, F.Cu at (230.1, 61.2)
- added J8: DISPLAY_PORT, Display_Port, F.Cu at (238.8, 218.4)
- added J9: DISPLAY_PORT, Display_Port, F.Cu at (265.4, 218.4)
- added U23: 24AA02E48, SO8E_N, F.Cu at (330.7, 249.2)
- added X1: CRYSTAL, HC-49V, F.Cu at (366.0, 208.0)
- C133, C140, C157, C161, C164, C81, U11: moved to B.Cu
- C79: moved to F.Cu
- P1: footprint pin_array_6x2_SMD -> ScrewTerm2
- moved U4 125.0 mm to (259.6, 84.3)
- moved P1 114.9 mm to (253.2, 63.2)
- moved C14 94.9 mm to (235.5, 164.8), turned to 0 degrees
- moved C11 94.8 mm to (235.5, 150.6), turned to 0 degrees
- moved C13 94.6 mm to (235.5, 163.5), turned to 0 degrees
- moved C6 94.6 mm to (235.5, 151.6), turned to 0 degrees
- moved C187 94.3 mm to (235.5, 162.5), turned to 0 degrees
- moved C2 94.3 mm to (235.5, 152.6), turned to 0 degrees
- moved C178 94.2 mm to (235.5, 161.5), turned to 0 degrees
- moved C5 94.1 mm to (235.5, 153.6), turned to 0 degrees
- moved C3 94.0 mm to (235.5, 160.5), turned to 0 degrees
- moved C9 94.0 mm to (235.5, 154.6), turned to 0 degrees
- moved C8 93.9 mm to (235.5, 155.9), turned to 0 degrees
- moved C4 93.9 mm to (235.5, 158.9), turned to 0 degrees
- moved C7 93.8 mm to (235.5, 156.9), turned to 0 degrees
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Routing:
- net (no net): track 1089.6 -> 3655.4 mm, vias 112 -> 120
- net GND: track 338.1 -> 561.4 mm, vias 151 -> 221
- net VCC1V5: track 100.3 -> 197.4 mm, vias 27 -> 39
- net VCC1V2: track 29.3 -> 86.5 mm, vias 20 -> 22
- net VCC12V0: track 0.00 -> 49.8 mm, vias 0 -> 15
- net /Power/Conference 12V: track 0.00 -> 45.4 mm
- net /DDR3/DDR0_A3: track 51.8 -> 6.90 mm
- net /DDR3/DDR0_DQ3: track 46.0 -> 1.14 mm
- net /DDR3/DDR0_DQ2: track 46.1 -> 1.19 mm
- net /DDR3/DDR0_DQ4: track 46.0 -> 1.21 mm
- net /DDR3/DDR0_A7: track 50.1 -> 5.34 mm
- net /DDR3/DDR0_DQ5: track 45.9 -> 1.19 mm
- net /DDR3/DDR0_DQ10: track 45.9 -> 1.25 mm
- net /DDR3/DDR0_CKE: track 47.7 -> 2.98 mm
- net /DDR3/DDR0_DQ8: track 45.9 -> 1.29 mm
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- added copper zone on B.Cu, net /Power/Conference 12V
- added copper zone on F.Cu, net /Power/Conference 12V
- added copper zone on B.Cu, net /Power/VIN 48
- added copper zone on F.Cu, net /Power/VIN 48
- added copper zone on B.Cu, net GND
- added copper zone on F.Cu, net GND
- added copper zone on F.Cu, net N-00000391
- added copper zone on F.Cu, net N-00000398
- added copper zone on F.Cu, net N-00000401
- added copper zone on F.Cu, net N-00000413
- added copper zone on B.Cu, net VCC12V0
- added copper zone on F.Cu, net VCC12V0
- added copper zone on B.Cu, net VCC1V2
- added copper zone on F.Cu, net VCC1V2
- added copper zone on B.Cu, net VCC1V5
- added copper zone on F.Cu, net VCC1V5
- added copper zone on B.Cu, net VCC3V3
- added copper zone on F.Cu, net VCC3V3

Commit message: Issue #1412 - Placement
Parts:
- added C172: 0.1mfd, SM0402, F.Cu at (201.4, 215.4)
- R137, R138, R139, R140, R141, R142, R143, R144, R146, R148, R149, R151, R153, R196, R197, R199, R204, R205: footprint SM0603 -> SM0402
- moved C39 121.1 mm to (335.0, 153.9)
- moved C40 121.1 mm to (335.0, 146.0)
- moved C41 121.1 mm to (334.0, 134.6)
- moved C44 121.1 mm to (347.2, 155.1)
- moved C52 121.1 mm to (347.2, 150.1)
- moved C53 121.1 mm to (347.2, 145.5)
- moved C54 121.1 mm to (347.2, 142.7)
- moved U2 121.1 mm to (341.1, 145.7)
- moved C42 121.1 mm to (337.6, 154.9)
- moved C43 121.1 mm to (335.3, 137.6)
- moved C58 121.1 mm to (345.9, 136.9)
- moved C66 121.1 mm to (342.9, 136.9)
- moved R21 115.4 mm to (55.2, 121.9)
- moved C171 115.4 mm to (49.4, 116.2)
- moved C36 115.4 mm to (54.5, 124.1)
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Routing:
- net (no net): track 3655.4 -> 819.2 mm, vias 120 -> 96
- net /Ethernet/ETH_RXD0: track 5.59 -> 135.9 mm, vias 1 -> 2
- net /Ethernet/ETH_RXD1: track 4.40 -> 132.0 mm, vias 1 -> 2
- net /Ethernet/ETH_RXD2: track 4.35 -> 126.7 mm, vias 1 -> 2
- net /DisplayPort/RX_LANEP0: track 0.78 -> 118.9 mm, vias 1 -> 2
- net /Ethernet/ETH_RXD3: track 6.05 -> 124.2 mm, vias 1 -> 2
- net /DisplayPort/RX_LANEN0: track 0.65 -> 117.2 mm, vias 1 -> 2
- net /DisplayPort/RX_LANEP1: track 0.53 -> 116.7 mm, vias 1 -> 2
- net /Ethernet/ETH_RXCTL: track 7.32 -> 123.4 mm, vias 1 -> 2
- net /DisplayPort/RX_LANEP2: track 0.69 -> 115.6 mm, vias 1 -> 2
- net /DisplayPort/RX_LANEN1: track 0.70 -> 115.0 mm, vias 1 -> 2
- net /Ethernet/ETH_RESET_B: track 5.22 -> 117.6 mm
- net /Ethernet/ETH_TXD0: track 1.56 -> 113.0 mm
- net /DisplayPort/RX_LANEN2: track 0.71 -> 112.1 mm, vias 1 -> 2
- net /Ethernet/ETH_TXD1: track 1.00 -> 111.1 mm
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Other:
- board text added: "HDMI IN 1"
- board text added: "HDMI IN 2"
- board text added: "HDMI OUT 1"
- board text added: "HDMI OUT 2"
